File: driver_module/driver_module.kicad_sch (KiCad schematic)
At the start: 113 parts, among them J1 Power Input, J19 Conn_01x03, J2 Power Input, J21 Power Input, J4 Conn_02x06_Odd_Even, J5 Conn_02x06_Odd_Even, J6 Conn_01x06, Q1 Q_PNP_BEC, Q2 Q_PNP_BEC, Q3 Q_PNP_BEC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

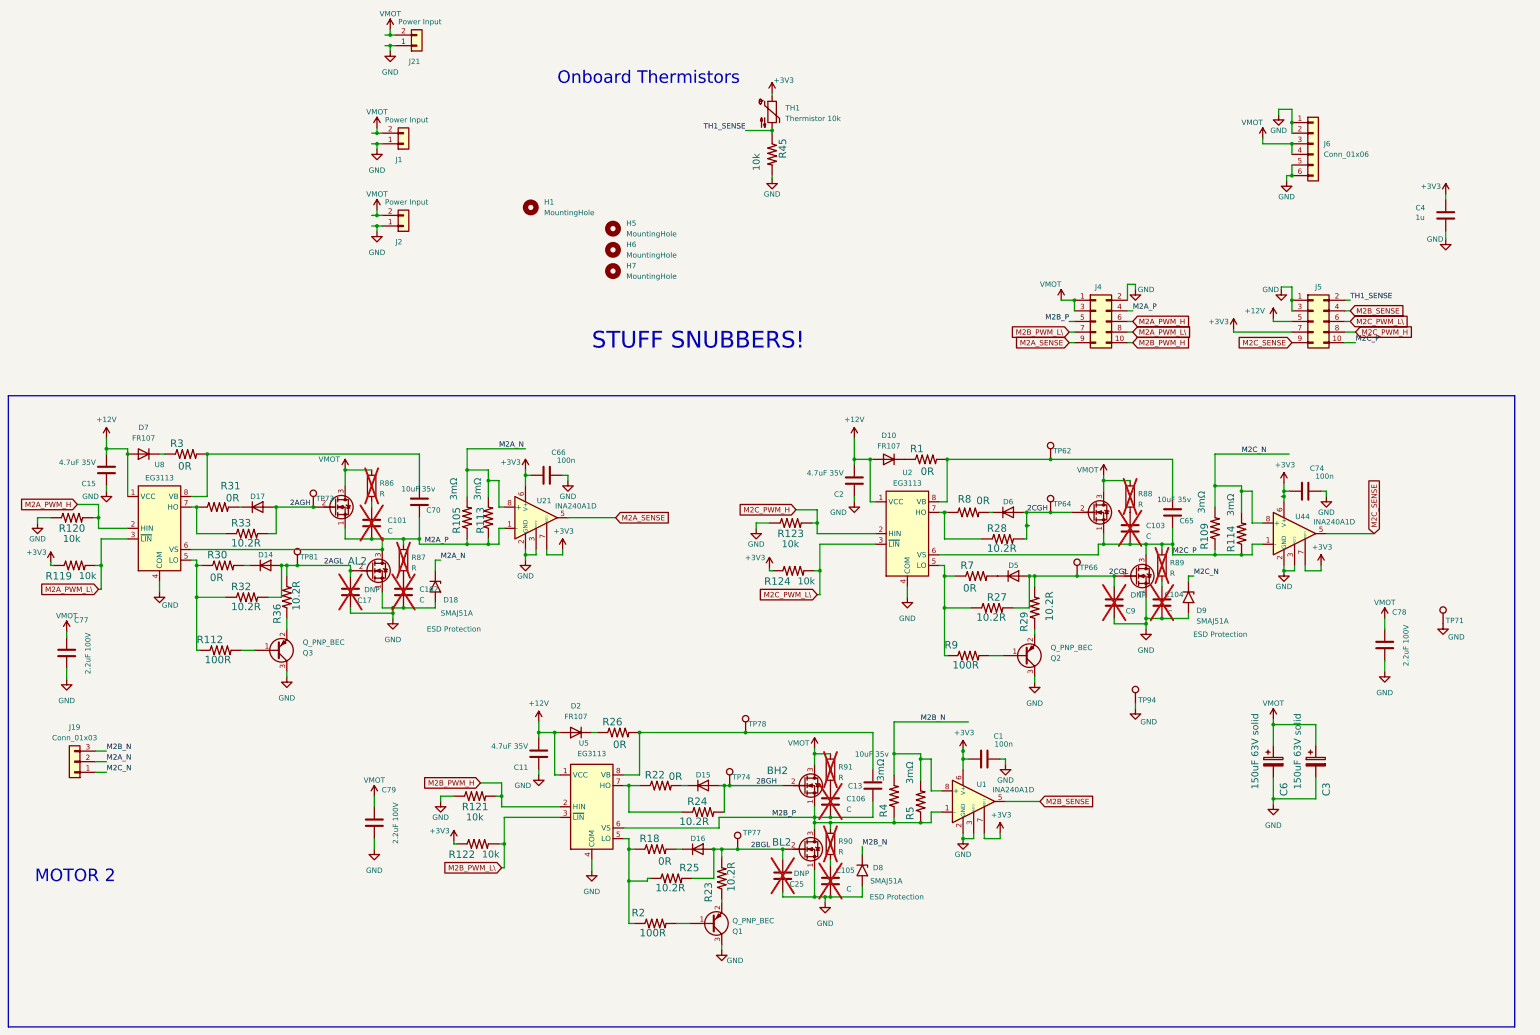
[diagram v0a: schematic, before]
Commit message: First pass responding to design review. Copper changes done but final review not complete.
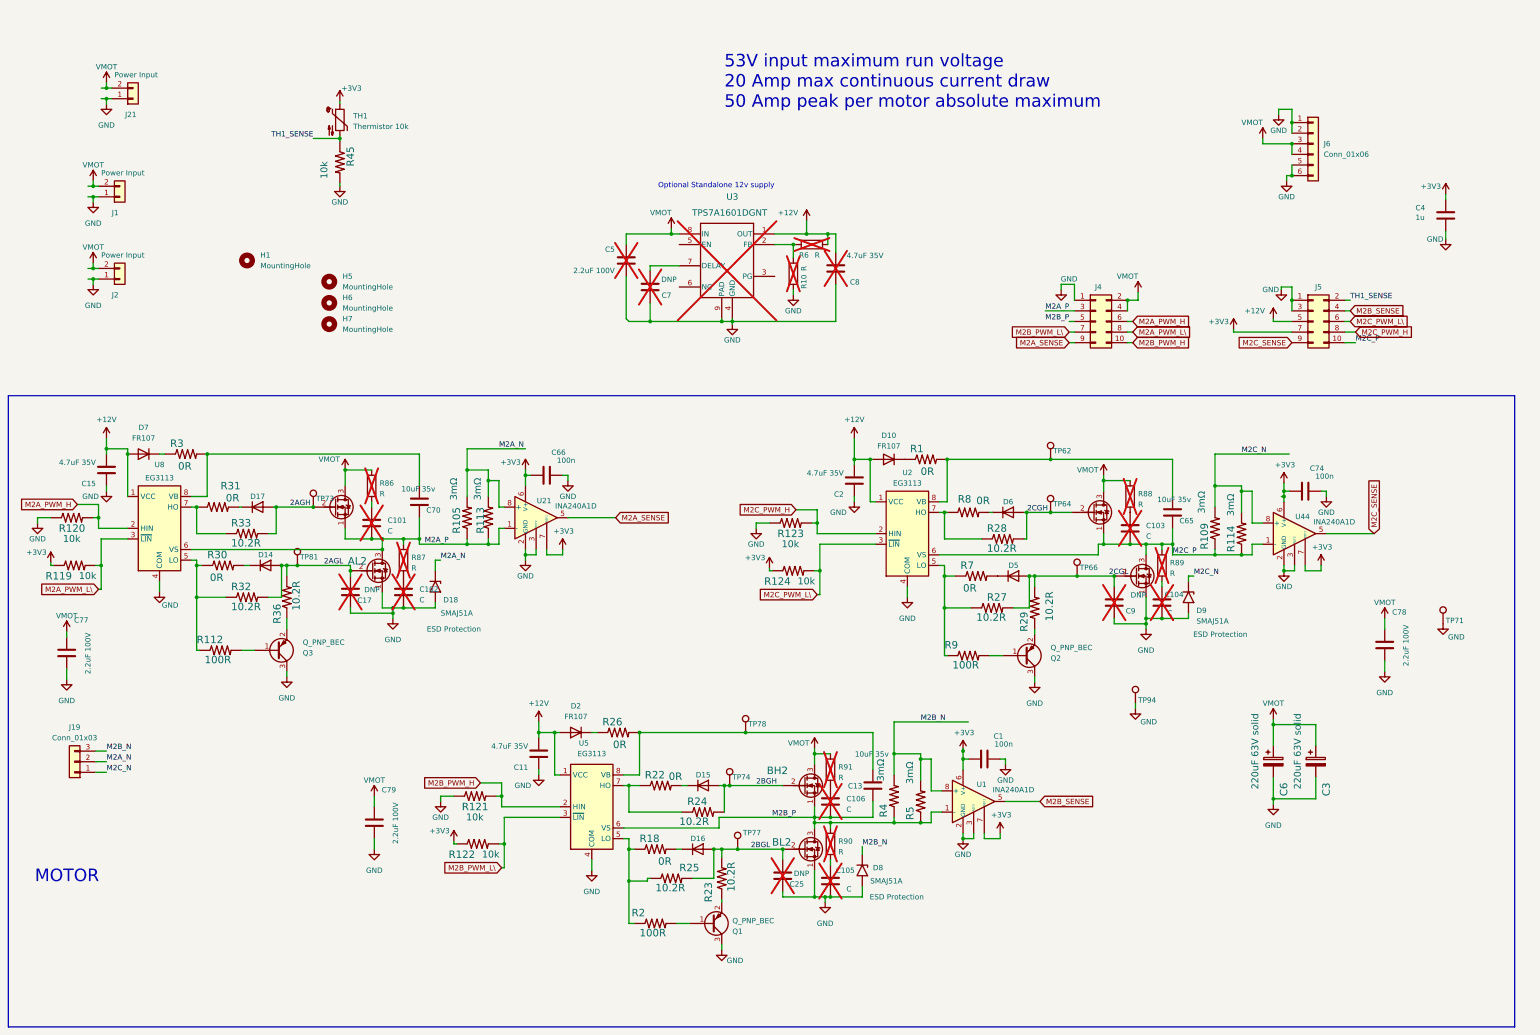
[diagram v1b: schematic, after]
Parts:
- added C5: 2.2uF 100V, Capacitor_SMD:C_0805_2012Metric, symbol Device:C
- added C7: DNP, Capacitor_SMD:C_0603_1608Metric, symbol Device:C
- added C8: 4.7uF 35V, Capacitor_SMD:C_0603_1608Metric, symbol Device:C
- added R10, R6: R, Capacitor_SMD:C_0603_1608Metric, symbol Device:R
- added U3: TPS7A1601DGNT, DGN0008C_N, symbol ldo:TPS7A1601DGNT
- C3, C6: value 150uF 63V solid -> 220uF 63V solid; LCSC C2983794 -> C2983797
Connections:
- net +12V: now also C8.2, R6.1, U3.1 (OUT)
- net GND: now also J4.1 (Pin_1), C5.2, C7.1, C8.1, R10.2, U3.4 (GND), U3.9 (PAD); no longer J4.2 (Pin_2)
- net M2A_P: now also J4.3 (Pin_3); no longer J4.4 (Pin_4)
- net VMOT: now also J4.2 (Pin_2), J4.4 (Pin_4), C5.1, U3.8 (IN); no longer J4.1 (Pin_1), J4.3 (Pin_3)
- new net: R10.1, R6.2, U3.2 (FB)
- new net: C7.2, U3.7 (DELAY)
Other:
- note added: "53V input maximum run voltage 20 Amp max continuous current draw 50 Amp peak per motor absolute maximum"
- note added: "MOTOR"
- note added: "Optional Standalone 12v supply"
- note removed: "MOTOR 2"
- note removed: "Onboard Thermistors"
- note removed: "STUFF SNUBBERS!"
- moved on the sheet: H1, H5, H6, H7, J1, J2, J21, R45, TH1

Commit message: Clean up of motor, base, and UI PCBs. Could be ready to order.
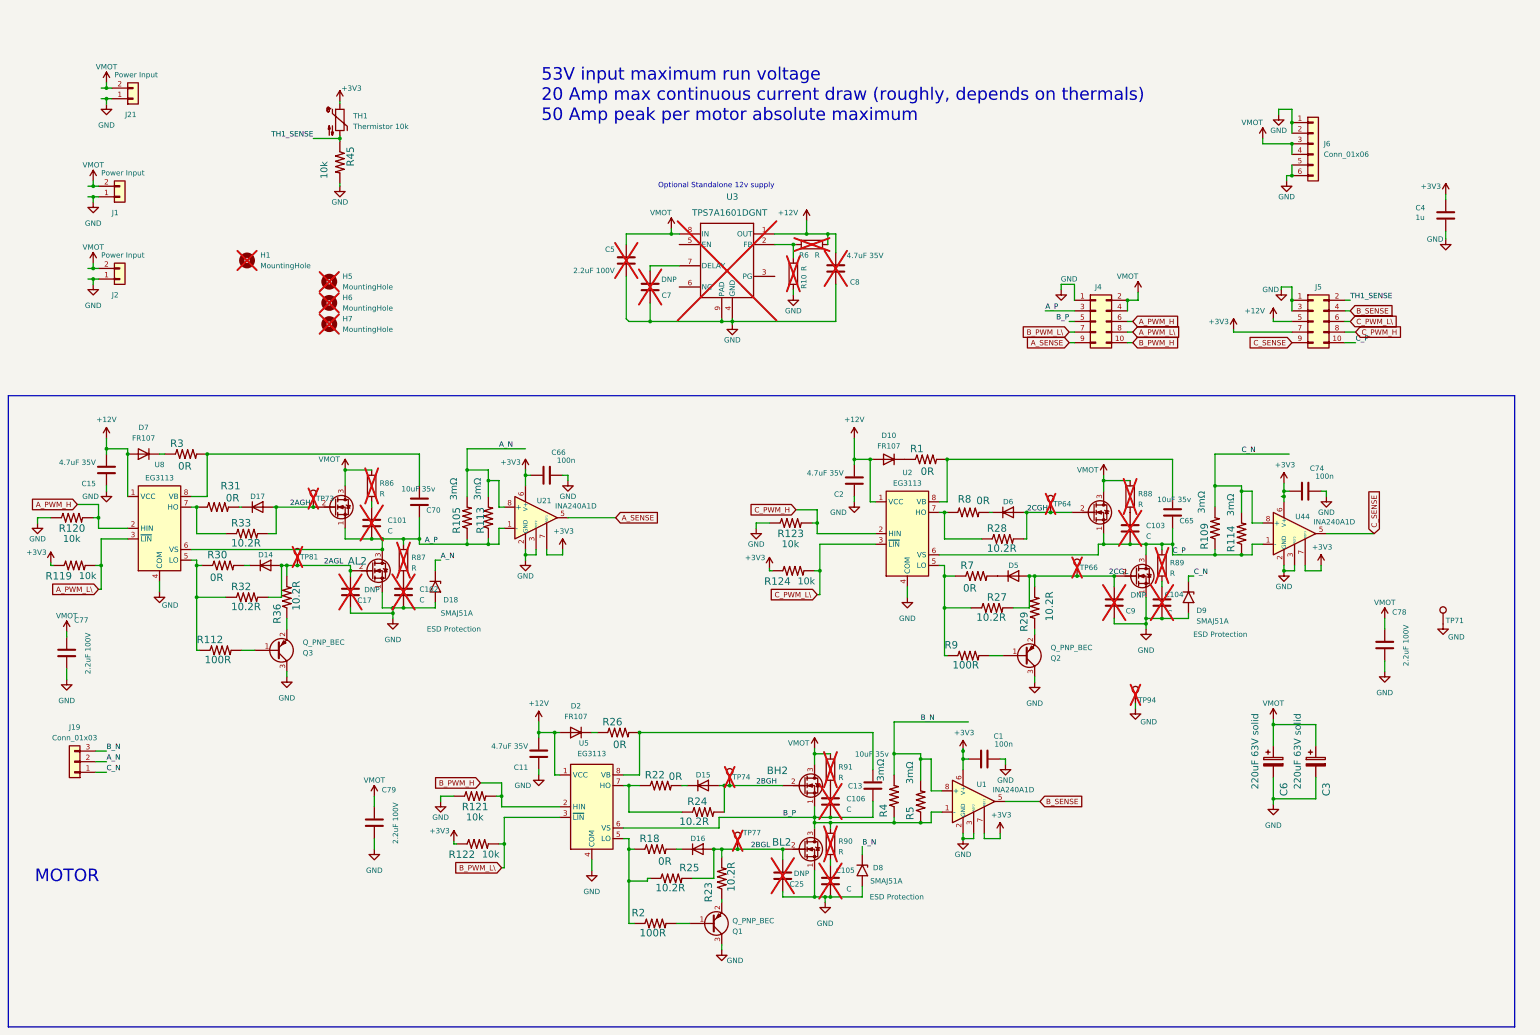
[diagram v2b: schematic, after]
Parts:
- removed TP62, TP78: TestPoint, parts:TestPoint_Pad_D1.5mm_no_courtyard, symbol Connector:TestPoint
- C101, C102, C103, C104, C105, C106, C17, C25, C7, C9, R86, R87, R88, R89, R90, R91: now in the parts list
- H1, H5, H6, H7, TP64, TP66, TP73, TP74, TP77, TP81, TP94: now not fitted; now in the parts list
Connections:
- net M2A_N renamed A_N
- net M2A_P renamed A_P
- net M2A_PWM_H renamed A_PWM_H
- net M2A_PWM_L\ renamed A_PWM_L\
- net M2A_SENSE renamed A_SENSE
- net M2B_N renamed B_N
- net M2B_P renamed B_P
- net M2B_PWM_H renamed B_PWM_H
- net M2B_PWM_L\ renamed B_PWM_L\
- net M2B_SENSE renamed B_SENSE
- net M2C_N renamed C_N
- net M2C_P renamed C_P
- net M2C_PWM_H renamed C_PWM_H
- net M2C_PWM_L\ renamed C_PWM_L\
- net M2C_SENSE renamed C_SENSE
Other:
- note added: "53V input maximum run voltage 20 Amp max continuous current draw (roughly, depends on thermals) 50 Amp peak per motor absolute maximum"
- note removed: "53V input maximum run voltage 20 Amp max continuous current draw 50 Amp peak per motor absolute maximum"

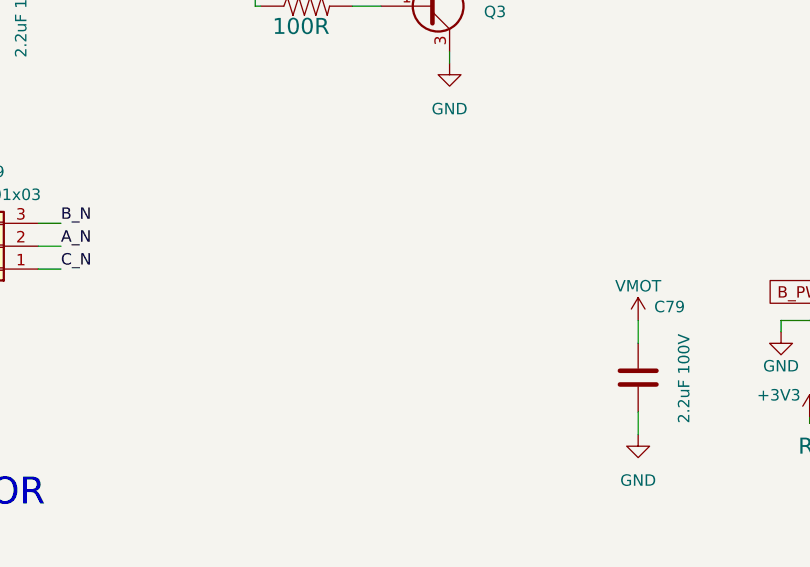
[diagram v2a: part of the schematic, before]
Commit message: Respond to latest round of design review.
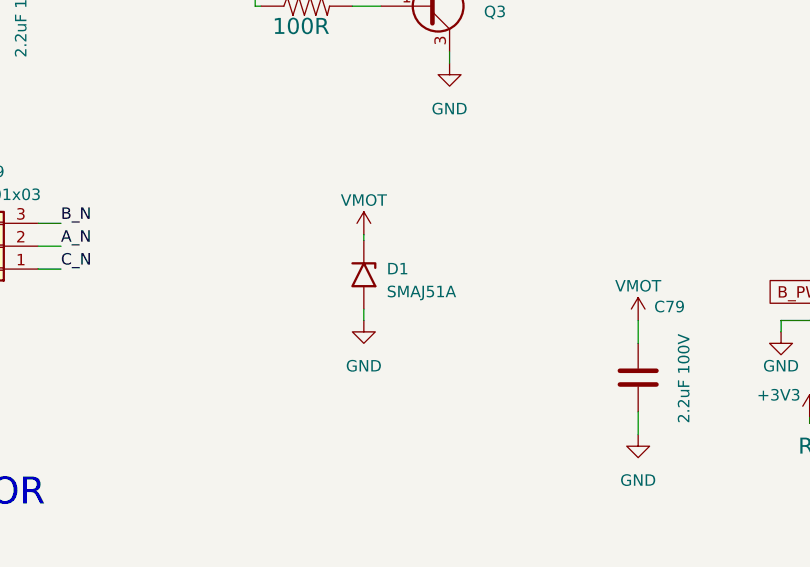
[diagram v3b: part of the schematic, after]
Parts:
- added D1: SMAJ51A, Diode_SMD:D_SMC, symbol Diode:SMF54A
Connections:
- net GND: now also D1.2 (A2)
- net VMOT: now also D1.1 (A1)
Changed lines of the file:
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@@
     (stroke (width 0) (type default))
   )
+  (wire (pts (xy 85.725 201.93) (xy 85.725 200.66))
+    (stroke (width 0) (type default))
+  )
   (wire (pts (xy 344.17 128.905) (xy 344.17 130.175))
     (stroke (width 0) (type default))
@@
     (stroke (width 0) (type default))
   )
+  (wire (pts (xy 85.725 192.405) (xy 85.725 193.04))
+    (stroke (width 0) (type default))
+  )
   (wire (pts (xy 203.2 214.63) (xy 213.995 214.63))
     (stroke (width 0) (type default))
@@
     )
   )
+  (symbol (lib_id "MotorBuck:VMOT") (at 85.725 192.405 0) (unit 1)
+    (in_bom yes) (on_board yes) (dnp no)
+    (property "Reference" "#PWR053" (at 85.725 196.215 0)
+      (effects (font (size 1.27 1.27)) hide)
+    )
+    (property "Value" "VMOT" (at 85.725 188.595 0)
+      (effects (font (size 1.27 1.27)))
+    )
+    (property "Footprint" "" (at 85.725 192.405 0)
+      (effects (font (size 1.27 1.27)) hide)
+    )
+    (property "Datasheet" "" (at 85.725 192.405 0)
+      (effects (font (size 1.27 1.27)) hide)
+    )
+    (property "Sim.Device" "SPICE" (at 85.725 196.215 0)
+      (effects (font (size 1.27 1.27)) hide)
+    )
+    (property "Sim.Params" "type=\"I\" model=\"VMOT\" lib=\"\"" (at -31.75 -26.67 0)
+      (effects (font (size 0 0)) hide)
+    )
+    (property "Sim.Pins" "1=1" (at -31.75 -26.67 0)
+      (effects (font (size 0 0)) hide)
+    )
+    (pin "1")
+    (instances
+      (project "driver_module"
+        (path "/889c04f7-ab14-429c-99d2-ed773c17e58f"
+          (reference "#PWR053") (unit 1)
+        )
+      )
+    )
+  )
   (symbol (lib_id "MotorController:TAYLOR_RESISTOR") (at 216.535 147.955 0) (unit 1)
     (in_bom yes) (on_board yes) (dnp no)
@@
     )
   )
+  (symbol (lib_id "power:GND") (at 85.725 201.93 0) (unit 1)
+    (in_bom yes) (on_board yes) (dnp no) (fields_autoplaced)
+    (property "Reference" "#PWR052" (at 85.725 208.28 0)
+      (effects (font (size 1.27 1.27)) hide)
+    )
+    (property "Value" "GND" (at 85.725 207.01 0)
+      (effects (font (size 1.27 1.27)))
+    )
+    (property "Footprint" "" (at 85.725 201.93 0)
+      (effects (font (size 1.27 1.27)) hide)
+    )
+    (property "Datasheet" "" (at 85.725 201.93 0)
+      (effects (font (size 1.27 1.27)) hide)
+    )
+    (pin "1")
+    (instances
+      (project "driver_module"
+        (path "/889c04f7-ab14-429c-99d2-ed773c17e58f"
+          (reference "#PWR052") (unit 1)
+        )
+      )
+    )
+  )
   (symbol (lib_id "MotorController:TAYLOR_RESISTOR") (at 85.725 139.065 0) (unit 1)
     (in_bom yes) (on_board yes) (dnp no)
@@
         )
       )
+    )
+  )
+  (symbol (lib_id "Diode:SMF54A") (at 85.725 196.85 270) (unit 1)
+    (in_bom yes) (on_board yes) (dnp no) (fields_autoplaced)
+    (property "Reference" "D1" (at 88.265 196.215 90)
+      (effects (font (size 1.27 1.27)) (justify left))
+    )
+    (property "Value" "SMAJ51A" (at 88.265 198.755 90)
+      (effects (font (size 1.27 1.27)) (justify left))
+    )
+    (property "Footprint" "Diode_SMD:D_SMC" (at 80.645 196.85 0)
+      (effects (font (size 1.27 1.27)) hide)
+    )
+    (property "Datasheet" "" (at 85.725 195.58 0)
+      (effects (font (size 1.27 1.27)) hide)
+    )
+    (property "LCSC" "C438169" (at 85.725 196.85 90)
+      (effects (font (size 1.27 1.27)) hide)
+    )
+    (pin "1")
+    (pin "2")
+    (instances
+      (project "driver_module"
+        (path "/889c04f7-ab14-429c-99d2-ed773c17e58f"
+          (reference "D1") (unit 1)
+        )
+      )

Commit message: Final files as ordered today for base, module, and UI
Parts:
- C5: DNP_LCSC (none) -> C2981733; LCSC C2981733 -> (none)
- C8: DNP_LCSC (none) -> C162274; LCSC C162274 -> (none)
- U3: DNP_LCSC (none) -> C2865275; LCSC C2865275 -> (none)
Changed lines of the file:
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@@
       (effects (font (size 1.27 1.27)) hide)
     )
-    (property "LCSC" "C162274" (at 226.695 75.565 0)
+    (property "DNP_LCSC" "C162274" (at 226.695 75.565 0)
       (effects (font (size 1.27 1.27)) hide)
     )
@@
       (effects (font (size 1.27 1.27)) hide)
     )
-    (property "LCSC" "C2981733" (at 176.53 73.66 0)
+    (property "DNP_LCSC" "C2981733" (at 176.53 73.66 0)
       (effects (font (size 1.27 1.27)) hide)
     )
@@
       (effects (font (size 1.27 1.27) italic) hide)
     )
-    (property "LCSC" "C2865275" (at 201.93 72.39 0)
-      (effects (font (size 1.27 1.27)) hide)
-    )
+    (property "DNP_LCSC" "C2865275" (at 201.93 72.39 0)
+      (effects (font (size 1.27 1.27)) hide)
+    )

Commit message: Update boards for latest build, pending design review.
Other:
- note added: "Note: Dual current sense resistors are used to allow for easier use at lower power levels. Remove one resistor or order boards with only one stuffed for more resolution at lower power."

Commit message: Change enable behavior and ensure low side FETs activate for hardware braking
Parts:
- U3: footprint DGN0008C_N -> parts:DGN0008C_N
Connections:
- net +3V3: no longer R119.1, R122.1, R124.1
- net GND: now also R119.1, R122.1, R124.1
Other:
- note added: "Changelog: July 16 2024 Change low side pullups to pulldowns so that low side FET is on by default."
- moved on the sheet: C103, C104, C2, C65, C74, C78, C9, D10, D5, D6, D9, Q2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

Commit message: Updated files for boards ordered July 2024
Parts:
- C3, C6: LCSC C2983797 -> C5455531; MPN (none) -> 2210631013R00
- D1: value SMAJ51A -> SMDJ51CA; LCSC C438169 -> C406702
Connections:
- net VMOT: now also U3.5 (EN)
- no-connect marks 0 -> 2
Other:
- note added: "TODO: Consider adding delayed 12v power to drivers as is done on the base board."
- moved on the sheet: AL2, BH2, BL2, C1, C101, C102, C105, C106, C11, C13, C15, C17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
